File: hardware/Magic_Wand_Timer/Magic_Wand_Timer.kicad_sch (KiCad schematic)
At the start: 29 parts, among them J1 Action Input, J2 Caddy In/Out, J3 Conn_01x02, Q1 SI2301CDS-T1-GE3, Q2 MMBT5551L, Q3 AS2302, U1 NE555D

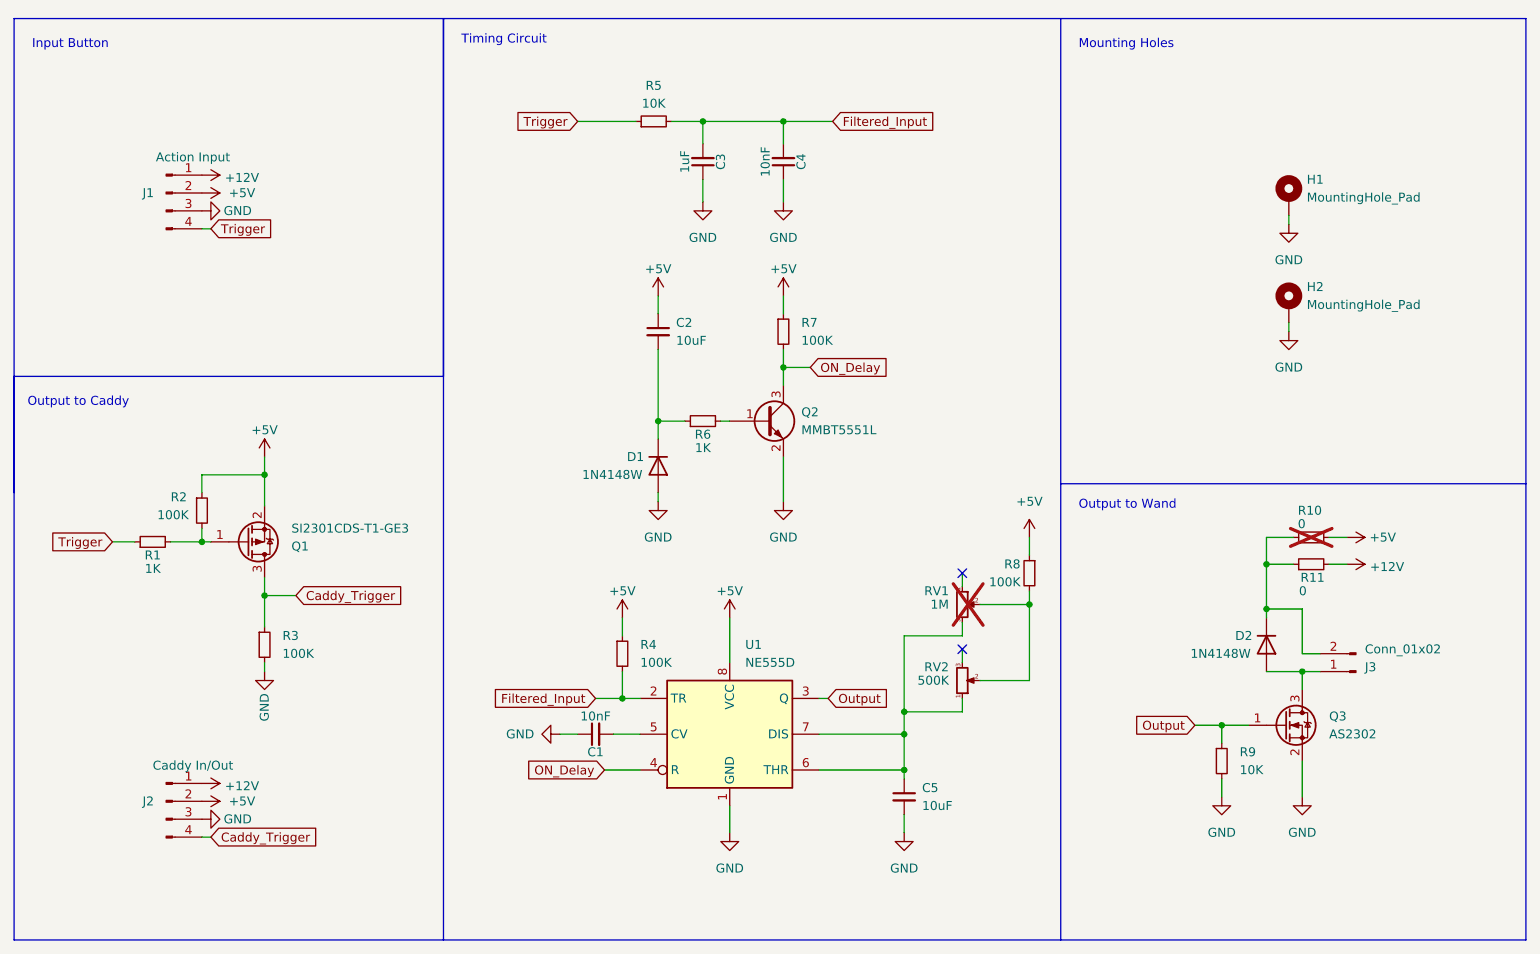
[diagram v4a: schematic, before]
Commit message: Update to Magic Wand Timer V4
Added decoupling capacitors, voltage select through polyfuse, moved connectors for load, caddy, button
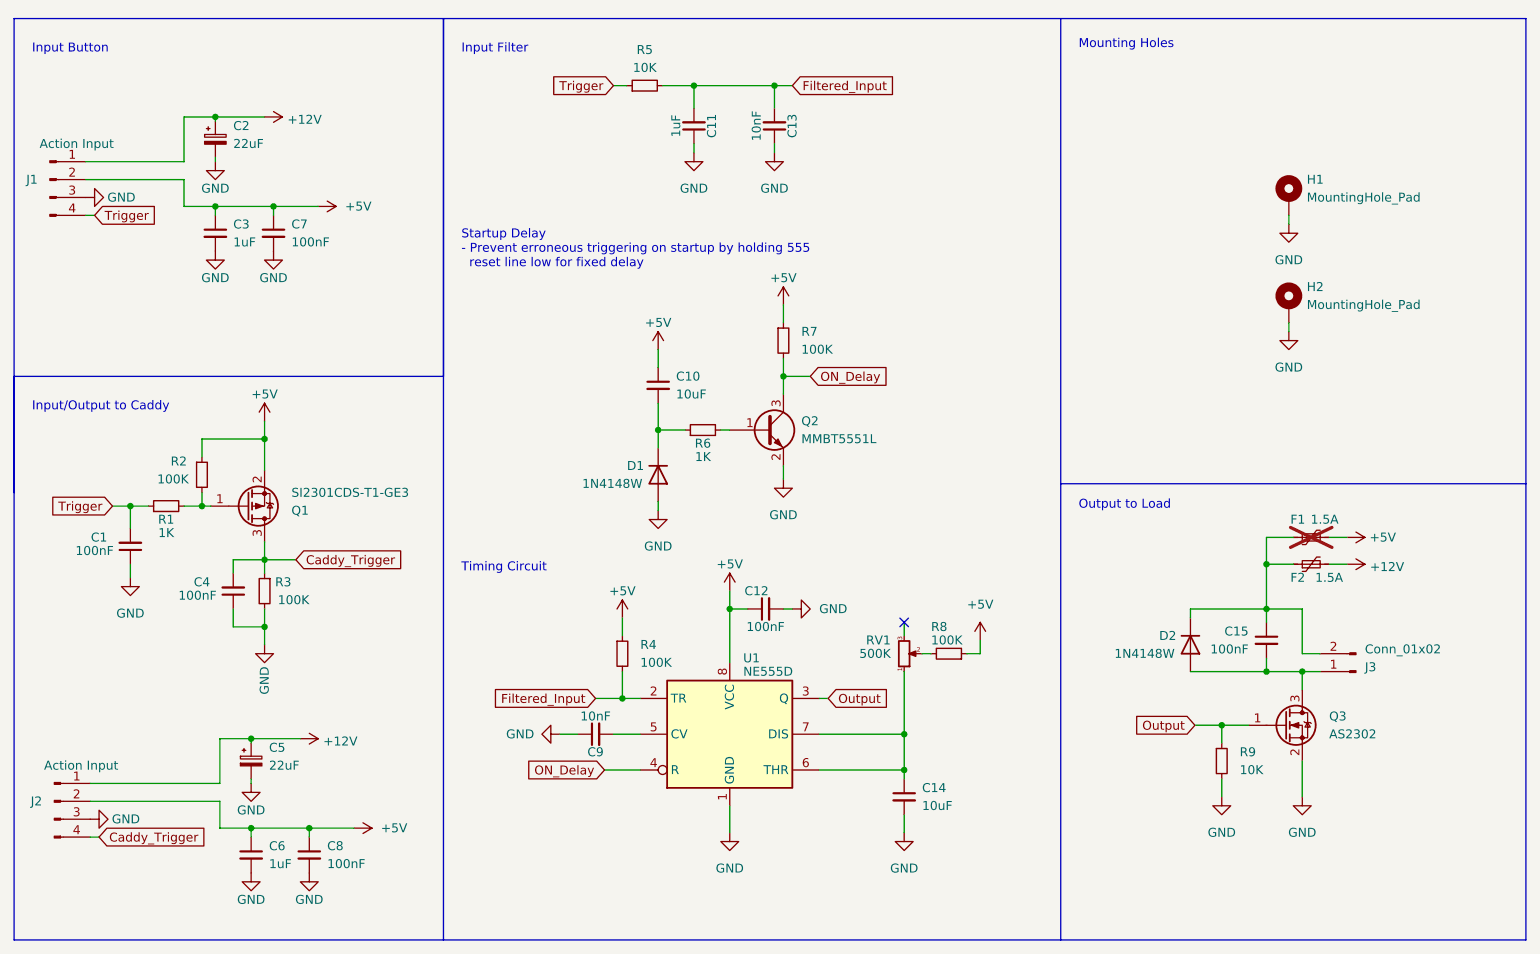
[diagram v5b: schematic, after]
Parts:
- removed R10, R11: 0, Resistor_SMD:R_0805_2012Metric, symbol Device:R_Small
- removed RV1: 1M, Potentiometer_THT:Potentiometer_Piher_PT-6-V_Vertical, symbol Device:R_Potentiometer_Small
- added C1, C12, C15, C4, C7, C8: 100nF, Capacitor_SMD:C_0603_1608Metric, symbol Device:C_Small
- added C2, C5: 22uF, Capacitor_THT:CP_Radial_D5.0mm_P2.00mm, symbol Device:C_Polarized_Small
- added C3, C6: 1uF, Capacitor_SMD:C_0603_1608Metric, symbol Device:C_Small
- added F1, F2: 1.5A, Fuse:Fuse_1210_3225Metric, symbol Device:Polyfuse_Small
- C11: renamed from C3; footprint Capacitor_SMD:C_0805_2012Metric -> Capacitor_SMD:C_0603_1608Metric; MPN C28323 -> C15849
- C13: renamed from C4; footprint Capacitor_SMD:C_0805_2012Metric -> Capacitor_SMD:C_0603_1608Metric; MPN C1710 -> C57112
- C9: renamed from C1; footprint Capacitor_SMD:C_0805_2012Metric -> Capacitor_SMD:C_0603_1608Metric; MPN C1710 -> C57112
- J2: value Caddy In/Out -> Action Input
- R1, R6: footprint Resistor_SMD:R_0805_2012Metric -> Resistor_SMD:R_0603_1608Metric; MPN C17513 -> C21190
- R2, R3, R4, R7, R8: footprint Resistor_SMD:R_0805_2012Metric -> Resistor_SMD:R_0603_1608Metric; MPN C149504 -> C25803
- R5, R9: footprint Resistor_SMD:R_0805_2012Metric -> Resistor_SMD:R_0603_1608Metric; MPN C17414 -> C25804
- renumbered C2 to C10, C5 to C14, RV2 to RV1
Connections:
- net +12V: now also C2.1, C5.1, F2.2
- net +5V: now also C12.1, C3.1, C6.1, C7.1, C8.1, F1.2
- net Caddy_Trigger: now also C4.2
- net GND: now also C1.1, C12.2, C2.2, C3.2, C4.1, C5.2, C6.2, C7.2, C8.2
- net Trigger: now also C1.2
- net at D2.1 (K), J3.2 (Pin_2): now also C15.1, F1.1, F2.1
- net at D2.2 (A), J3.1 (Pin_1), Q3.3 (D): now also C15.2
- no-connect marks 2 -> 1
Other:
- note added: "Input Filter"
- note added: "Input/Output to Caddy"
- note added: "Output to Load"
- note added: "Startup Delay - Prevent erroneous triggering on startup by holding 555 reset line low for fixed delay"
- note removed: "Output to Caddy"
- note removed: "Output to Wand"
- moved on the sheet: C10, C11, C13, D1, D2, J1, Q1, Q2, R1, R2, R3, R5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
